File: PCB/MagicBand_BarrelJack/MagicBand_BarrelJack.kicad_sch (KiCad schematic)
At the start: 19 parts, among them J2 MFRC522_Module, J3 RF_TX_DFLIFE, J6 NeoPixel_LED_Strip, J8 PWR_IN_BarrelJack_BareLeads, J9 ISP_AVR_2x3, Q1 AO3401A_PMOS_G-S-D, U1 ATmega328P-P, U2 MCP1700-3302, Y1 16MHz

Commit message: J9: reassign footprint to shrouded IDC-6 box header (schematic only)
Switched J9's footprint field from a plain PinHeader_2x03 to
Connector_IDC:IDC-Header_2x03_P2.54mm_Vertical -- a keyed/shrouded
box header, so future ISP programming uses a foolproof ribbon-cable
connector instead of 6 loose jumper wires. ERC still 0 errors /
129 pre-existing warnings, unaffected.

PCB-side placement NOT done here: the shrouded part's physical body
is much larger than the plain header (~10x16mm incl. shroud) and
does not fit at J9's current position (9,4) -- it would overhang the
board's top edge by ~1.6mm and crowd J2's courtyard. Needs a GUI
reposition + reroute of 6 short nets (D11/D12/D13/RESET/+5V/GND).
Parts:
- J9: footprint Connector_PinHeader_2.54mm:PinHeader_2x03_P2.54mm_Vertical -> Connector_IDC:IDC-Header_2x03_P2.54mm_Vertical
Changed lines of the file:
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@@
 			(effects (font (size 1.27 1.27)))
 		)
-		(property "Footprint" "Connector_PinHeader_2.54mm:PinHeader_2x03_P2.54mm_Vertical"
+		(property "Footprint" "Connector_IDC:IDC-Header_2x03_P2.54mm_Vertical"
 			(at 140 190 0)
 			(effects (font (size 1.27 1.27)) (hide yes))

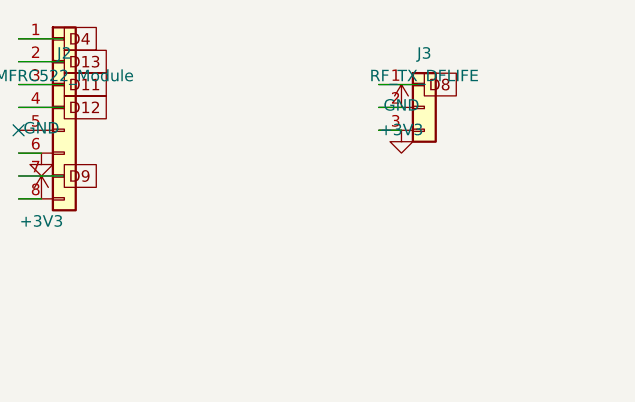
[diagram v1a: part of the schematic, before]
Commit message: Add RF TX/RX loopback bench-test sketch, J3 schematic prep for Enable pin, blank stop-sketch
RF_TXRX_Loopback: bench-validates the TX module by decoding its own
transmission on a second RX module, wired to the same board. Confirmed the
TX radiates a correct, decodable signal (matches the real remote's captured
code byte-for-byte) even at point-blank range to the target outlet, which
still doesn't respond -- narrows the open question toward the physical TX
module itself (frequency drift, weak output) or the outlet needing a
learn/pair step, rather than protocol/timing correctness.

Also fixed a real bug along the way: don't insert an artificial gap between
manually-spaced repeats -- rc-switch's receiveProtocol() uses the gap
duration to self-calibrate its assumed pulse-length unit
(delay = timings[0] / syncLengthInPulses), so a gap much longer than the
protocol's native sync period (~7ms at protocol 2 / 700us pulses, not the
133ms first tried) makes every subsequent bit comparison fail. Sending
repeats as separate calls with no added delay (letting each call's own
native trailing sync provide the separation) fixed it.

RF_TX_Test/Blank: trivial empty sketch, used to immediately stop an
RF_TX_Test board mid-session by reflashing over it (auto-reset on upload
beats waiting for a serial command).

MagicBand_BarrelJack.kicad_sch: J3 (RF TX module connector) changed from a
3-pin to 4-pin header, with the new pin 4 wired as an explicit no-connect
representing the module's physical Enable pin (confirmed non-functional
per the vendor listing, but present and pre-soldered on the physical
module). ERC-clean, matches pre-edit baseline exactly (129/129 violations,
all pre-existing). PCB-side footprint placement is still an open decision --
J3 sits close enough to the board edge that a real 4th pad for Enable would
land off-board; the two options on the table are skip the pad and clip the
physical pin during assembly, or move J3 inward and reroute its 3 nets.
Not yet resolved.
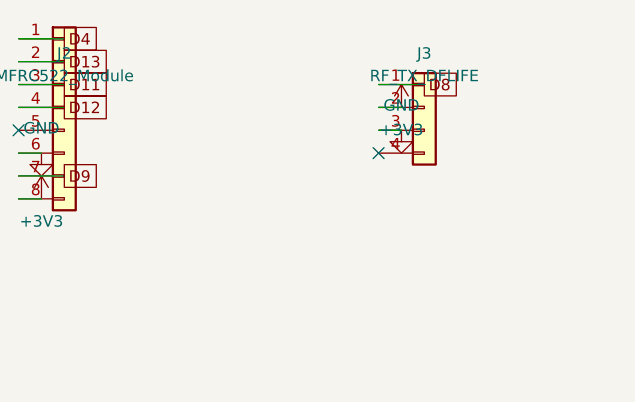
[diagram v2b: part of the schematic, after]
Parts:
- J3: footprint Connector_PinHeader_2.54mm:PinHeader_1x03_P2.54mm_Vertical -> Connector_PinHeader_2.54mm:PinHeader_1x04_P2.54mm_Vertical; symbol Connector_Generic:Conn_01x03 -> Connector_Generic:Conn_01x04
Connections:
- no-connect marks 13 -> 14
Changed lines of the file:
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@@
 	)
 	(symbol
-		(lib_id "Connector_Generic:Conn_01x03")
+		(lib_id "Connector_Generic:Conn_01x04")
 		(at 290 40 0)
 		(unit 1)
@@
 			(effects (font (size 1.27 1.27)))
 		)
-		(property "Footprint" "Connector_PinHeader_2.54mm:PinHeader_1x03_P2.54mm_Vertical"
+		(property "Footprint" "Connector_PinHeader_2.54mm:PinHeader_1x04_P2.54mm_Vertical"
 			(at 290 40 0)
 			(effects (font (size 1.27 1.27)) (hide yes))
@@
 		(pin "2")
 		(pin "3")
+		(pin "4")
 		(instances
 			(project "MagicBand_BarrelJack"
@@
 		)
 	)
+	(no_connect (at 284.92 45.08))
 	(wire
 		(pts (xy 284.92 37.46) (xy 290.0 37.46))
